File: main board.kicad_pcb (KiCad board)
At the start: 2 copper layers, 159 x 146 mm, 118 parts, among them J1 #15, J10 #11, J11 #14, J12 #37, J13 #3, J14 #23, J15 #33, J16 #38, J17 #4, J18 #13, J19 #9, J2 Red-Blk, J20 #18, J21 #22, J22 #21, J23 #25, J24 #8, J25 #16, J26 #12, J27 #35, J28 #7, J29 #19, J3 #2, J30 #26, J31 #5, J32 #28, J33 #32, J34 #39, J35 #27, J36 #40, J37 #17, J38 #20, J39 #24, J4 Blk, J40 #29, J41 #30, J42 #31, J43 #34, J44 #36, J45 #Brn, J46 #Blu, J47 #41, J48 LED conn, J49 #42 1.5V, J5 #1, J50 #6.3V, J51 #6.3V, J6 #6, J7 #10, J8 Red-Yel, J9 Red-Grn, Q1 2N2907, Q2 BD136, Q3 PN2222A, Q4 DMP4010SK3Q, U1 6AL5, U2 ECC83

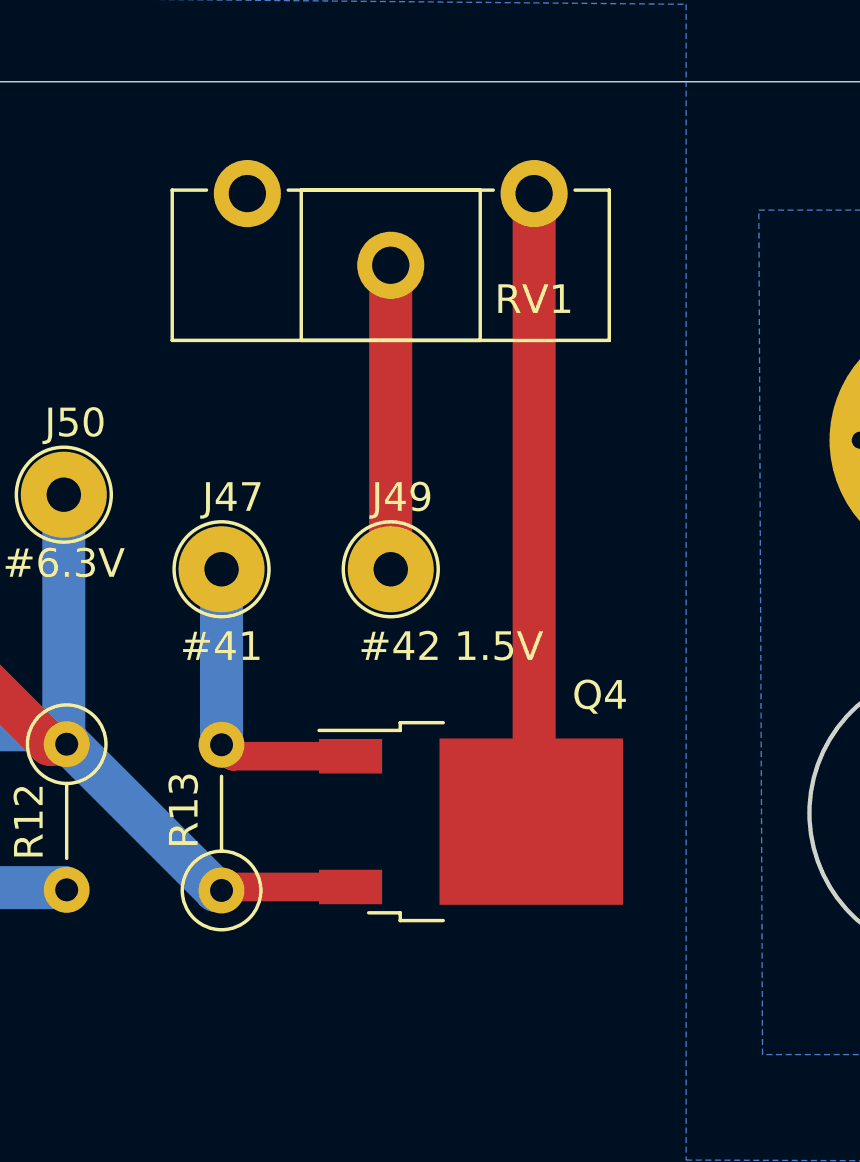
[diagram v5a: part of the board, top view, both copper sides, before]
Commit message: Use PNP as a switch
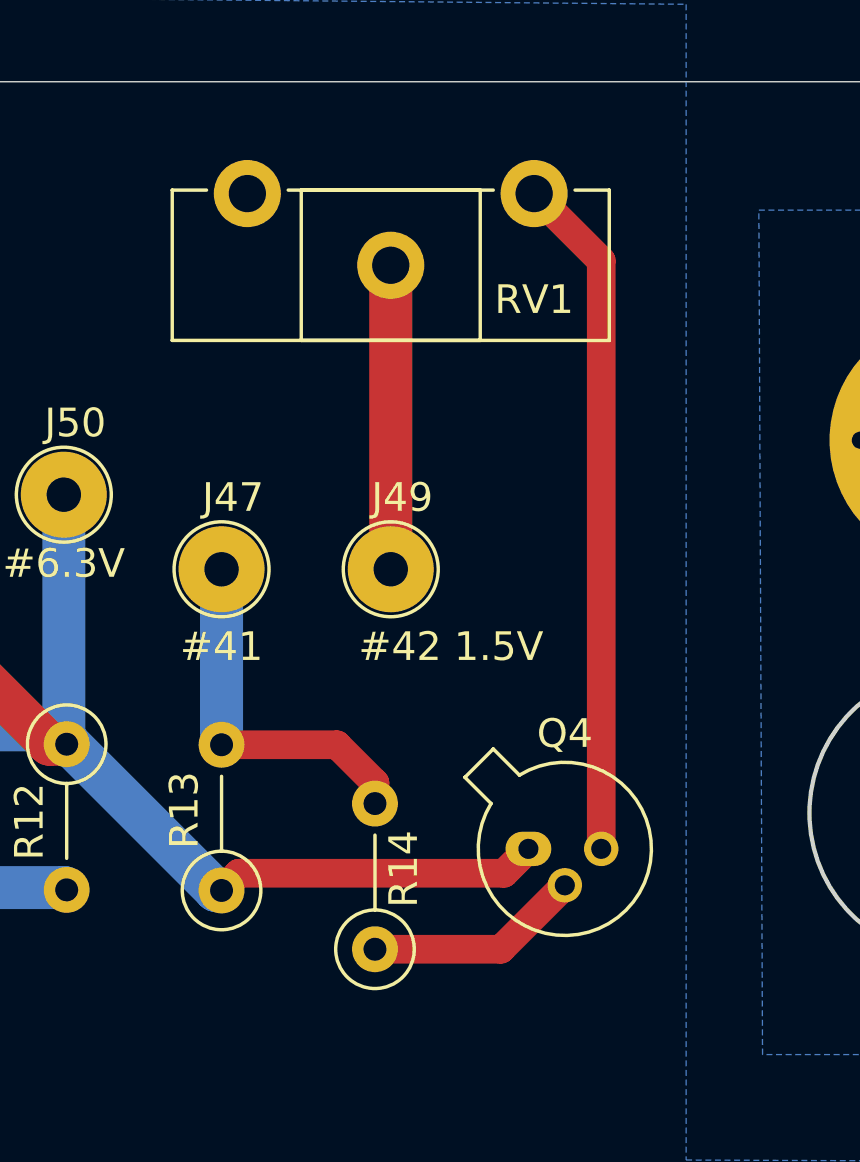
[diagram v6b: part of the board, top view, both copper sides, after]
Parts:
- added R14: 1k, Resistor_THT:R_Axial_DIN0207_L6.3mm_D2.5mm_P5.08mm_Vertical, F.Cu at (223.2, 92.5)
- Q4: value DMP4010SK3Q -> 2N2907; footprint Package_TO_SOT_SMD:TO-252-2 -> Package_TO_SOT_THT:TO-18-3
- moved Q4 2.21 mm to (228.5, 89.0)
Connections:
- Q4 pad 1: Net-(J47-Pad1) -> Net-(C11-Pad1)
- Q4 pad 3: Net-(C11-Pad1) -> Net-(Q4-Pad3)
- RV1 pad 1: Net-(Q4-Pad2) -> Net-(Q4-Pad3)
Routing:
- net Net-(Q4-Pad3): track 0.00 -> 23.8 mm
- net Net-(Q4-Pad2): track 21.9 -> 7.54 mm
- net Net-(C11-Pad1): track 65.1 -> 71.8 mm
- net Net-(J47-Pad1): track 10.8 -> 12.7 mm

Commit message: Rotate main BJT correctly
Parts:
- moved Q2 5.14 mm to (197.0, 73.0), turned to 0 degrees
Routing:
- net Net-(C9-Pad1): track 86.4 -> 76.2 mm
- net Net-(Q2-Pad3): track 10.5 -> 17.9 mm
- net Net-(C11-Pad1): track 71.8 -> 71.1 mm
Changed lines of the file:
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@@
     (thickness 1.6)
     (drawings 61)
-    (tracks 331)
+    (tracks 330)
     (zones 0)
     (modules 119)
@@
     (47 F.CrtYd user)
     (48 B.Fab user)
-    (49 F.Fab user)
+    (49 F.Fab user hide)
   )
   (setup
@@
   )
   (module Package_TO_SOT_THT:TO-126-3_Vertical (layer F.Cu)
-    (at 202.04 72.2 180)
+    (at 196.96 72.95)
     (descr "TO-126-3, Vertical, RM 2.54mm, see https://www.diodes.com/assets/Package-Files/TO126.pdf")
     (tags "TO-126-3 Vertical RM 2.54mm")
@@
       (effects (font (size 1 1) (thickness 0.15)))
     )
-    (pad 3 thru_hole oval (at 5.08 0 180) (size 1.8 1.8) (drill 1) (layers *.Cu *.Mask)
+    (pad 3 thru_hole oval (at 5.08 0) (size 1.8 1.8) (drill 1) (layers *.Cu *.Mask)
       (net 58 "Net-(Q2-Pad3)"))
-    (pad 2 thru_hole oval (at 2.54 0 180) (size 1.8 1.8) (drill 1) (layers *.Cu *.Mask)
+    (pad 2 thru_hole oval (at 2.54 0) (size 1.8 1.8) (drill 1) (layers *.Cu *.Mask)
       (net 59 "Net-(C11-Pad1)"))
-    (pad 1 thru_hole rect (at 0 0 180) (size 1.8 1.8) (drill 1) (layers *.Cu *.Mask)
+    (pad 1 thru_hole rect (at 0 0) (size 1.8 1.8) (drill 1) (layers *.Cu *.Mask)
       (net 50 "Net-(C9-Pad1)"))
     (model ${KISYS3DMOD}/Package_TO_SOT_THT.3dshapes/TO-126-3_Vertical.wrl
@@
   (segment (start 174.8 65) (end 156.12 65) (width 1.5) (layer B.Cu) (net 50))
   (segment (start 175.507898 65.707898) (end 174.8 65) (width 1.5) (layer B.Cu) (net 50) (status 10))
-  (segment (start 176.307897 64.907899) (end 175.507898 65.707898) (width 1.5) (layer B.Cu) (net 50))
-  (segment (start 201.257899 64.907899) (end 176.307897 64.907899) (width 1.5) (layer B.Cu) (net 50))
-  (segment (start 203.2 66.85) (end 201.257899 64.907899) (width 1.5) (layer B.Cu) (net 50))
-  (segment (start 203.2 71.04) (end 203.2 66.85) (width 1.5) (layer B.Cu) (net 50))
-  (segment (start 202.04 72.2) (end 203.2 71.04) (width 1.5) (layer B.Cu) (net 50))
+  (segment (start 186.207898 65.707898) (end 175.507898 65.707898) (width 1) (layer B.Cu) (net 50))
+  (segment (start 193.45 72.95) (end 186.207898 65.707898) (width 1) (layer B.Cu) (net 50))
+  (segment (start 196.96 72.95) (end 193.45 72.95) (width 1) (layer B.Cu) (net 50))
   (segment (start 157.9 68.3) (end 162.42 68.3) (width 1.5) (layer B.Cu) (net 51) (status 30))
   (segment (start 181.98 87.2) (end 181.98 78.58) (width 2) (layer B.Cu) (net 52) (status 10))
@@
   (segment (start 205.8 89.1) (end 207.3 89.1) (width 1.5) (layer B.Cu) (net 56) (status 10))
   (segment (start 223.7 79.3) (end 223.7 68.7) (width 1.5) (layer F.Cu) (net 57) (status 30))
-  (segment (start 189.80501 79.35499) (end 189.40501 79.35499) (width 1.5) (layer F.Cu) (net 58))
-  (segment (start 196.96 72.2) (end 189.80501 79.35499) (width 1.5) (layer F.Cu) (net 58))
+  (segment (start 202.04 76.96) (end 202.04 72.95) (width 1) (layer F.Cu) (net 58))
+  (segment (start 199.44 79.56) (end 202.04 76.96) (width 1) (layer F.Cu) (net 58))
+  (segment (start 189.2 79.56) (end 199.44 79.56) (width 1) (layer F.Cu) (net 58))
   (segment (start 191.79499 84.9) (end 189.2 82.30501) (width 1.5) (layer B.Cu) (net 59) (status 20))
   (segment (start 198.2 84.9) (end 191.79499 84.9) (width 1.5) (layer B.Cu) (net 59) (status 10))
@@
   (segment (start 211.8 85.4) (end 207.6 81.2) (width 1.5) (layer F.Cu) (net 59))
   (segment (start 212.4 85.4) (end 211.8 85.4) (width 1.5) (layer F.Cu) (net 59))
-  (segment (start 199.5 83.6) (end 198.2 84.9) (width 1.5) (layer F.Cu) (net 59))
-  (segment (start 199.5 72.2) (end 199.5 83.6) (width 1.5) (layer F.Cu) (net 59))
   (segment (start 227.65 89.9) (end 218.4 89.9) (width 1) (layer F.Cu) (net 59))
   (segment (start 218.4 89.9) (end 217.8 90.5) (width 1) (layer F.Cu) (net 59))
   (segment (start 228.5 89.05) (end 227.65 89.9) (width 1) (layer F.Cu) (net 59))
+  (segment (start 199.5 83.6) (end 198.2 84.9) (width 1) (layer B.Cu) (net 59))
+  (segment (start 199.5 72.95) (end 199.5 83.6) (width 1) (layer B.Cu) (net 59))
   (segment (start 227.54 92.55) (end 223.15 92.55) (width 1) (layer F.Cu) (net 60))
   (segment (start 229.77 90.32) (end 227.54 92.55) (width 1) (layer F.Cu) (net 60))

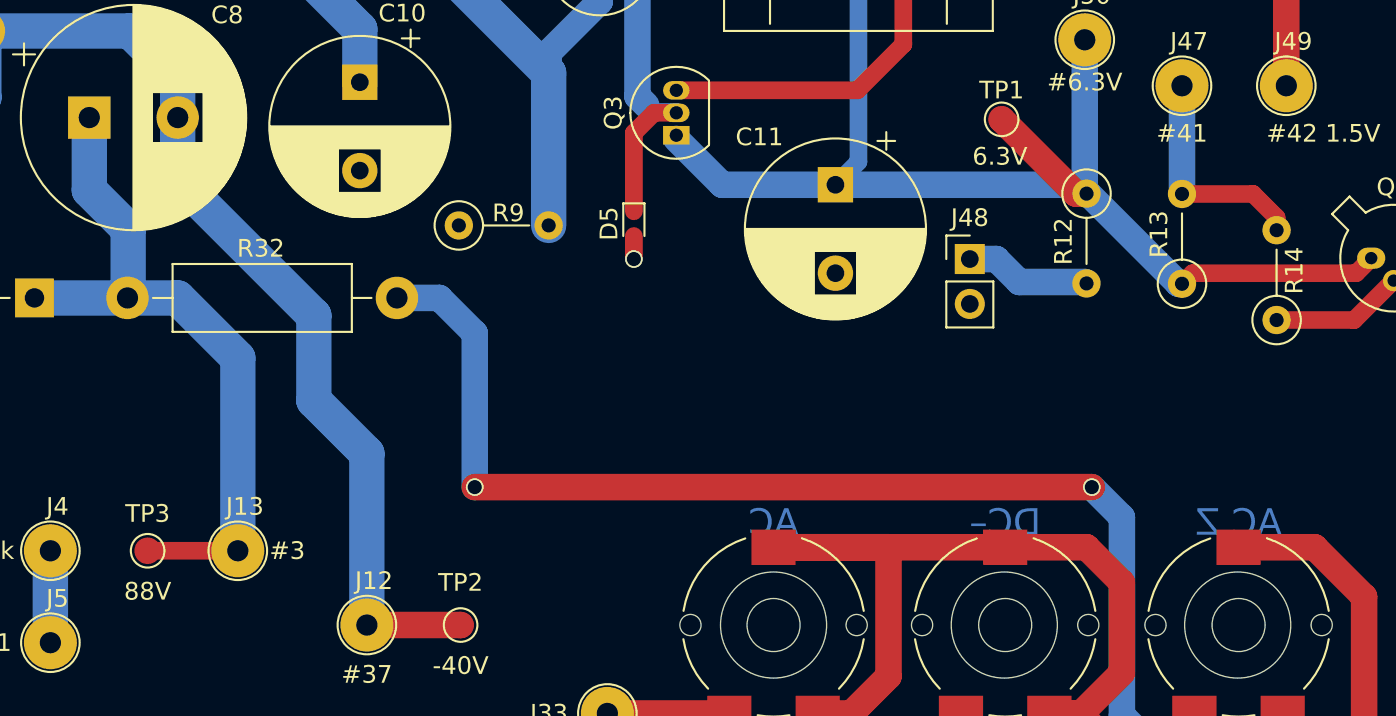
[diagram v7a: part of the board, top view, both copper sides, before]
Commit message: Add missing values after check
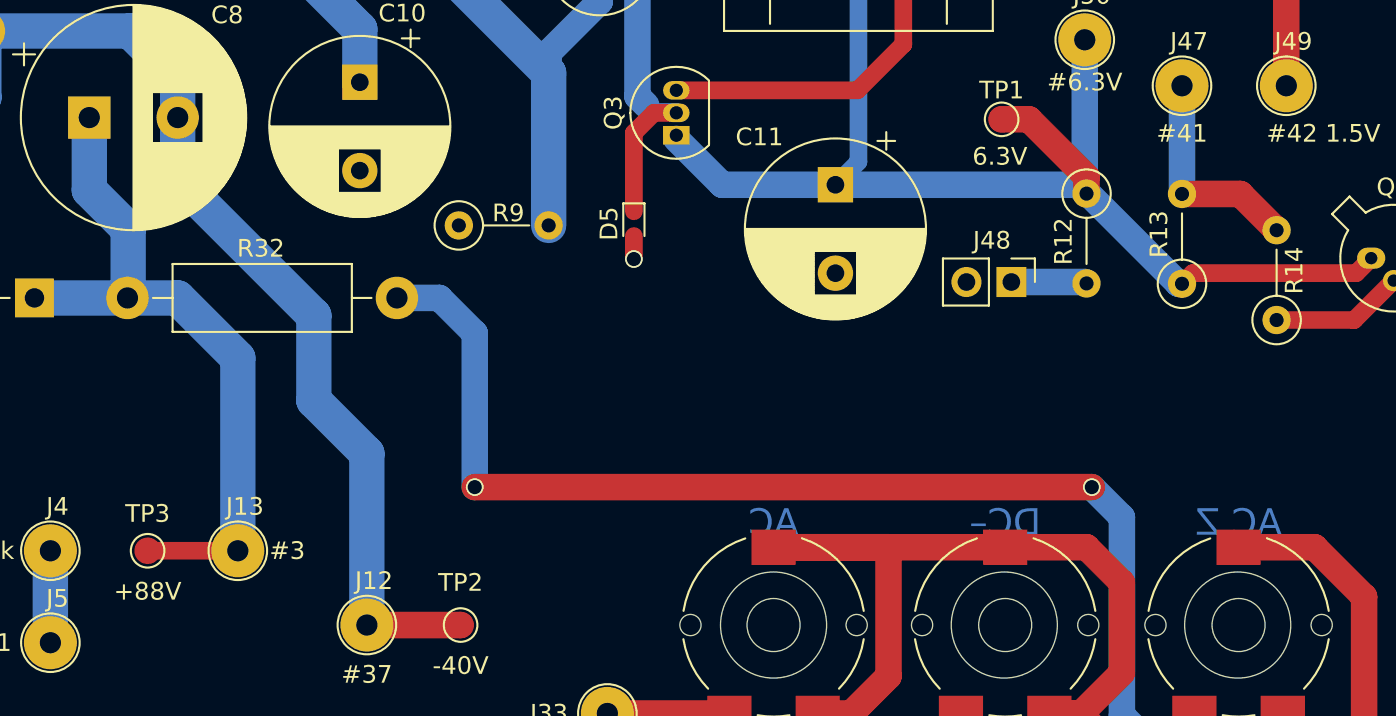
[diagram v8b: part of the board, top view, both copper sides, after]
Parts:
- R11: value 100 -> 33
- RV19, RV20, RV21, RV33: value R_POT -> 10k
- TP3: value 88V -> +88V
- moved J48 2.69 mm to (208.2, 90.4), turned to 270 degrees
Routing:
- net Net-(J48-Pad1): track 7.17 -> 4.28 mm
- net Net-(C11-Pad1): track 71.1 -> 71.6 mm
